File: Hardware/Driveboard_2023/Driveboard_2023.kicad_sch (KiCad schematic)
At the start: 15 parts

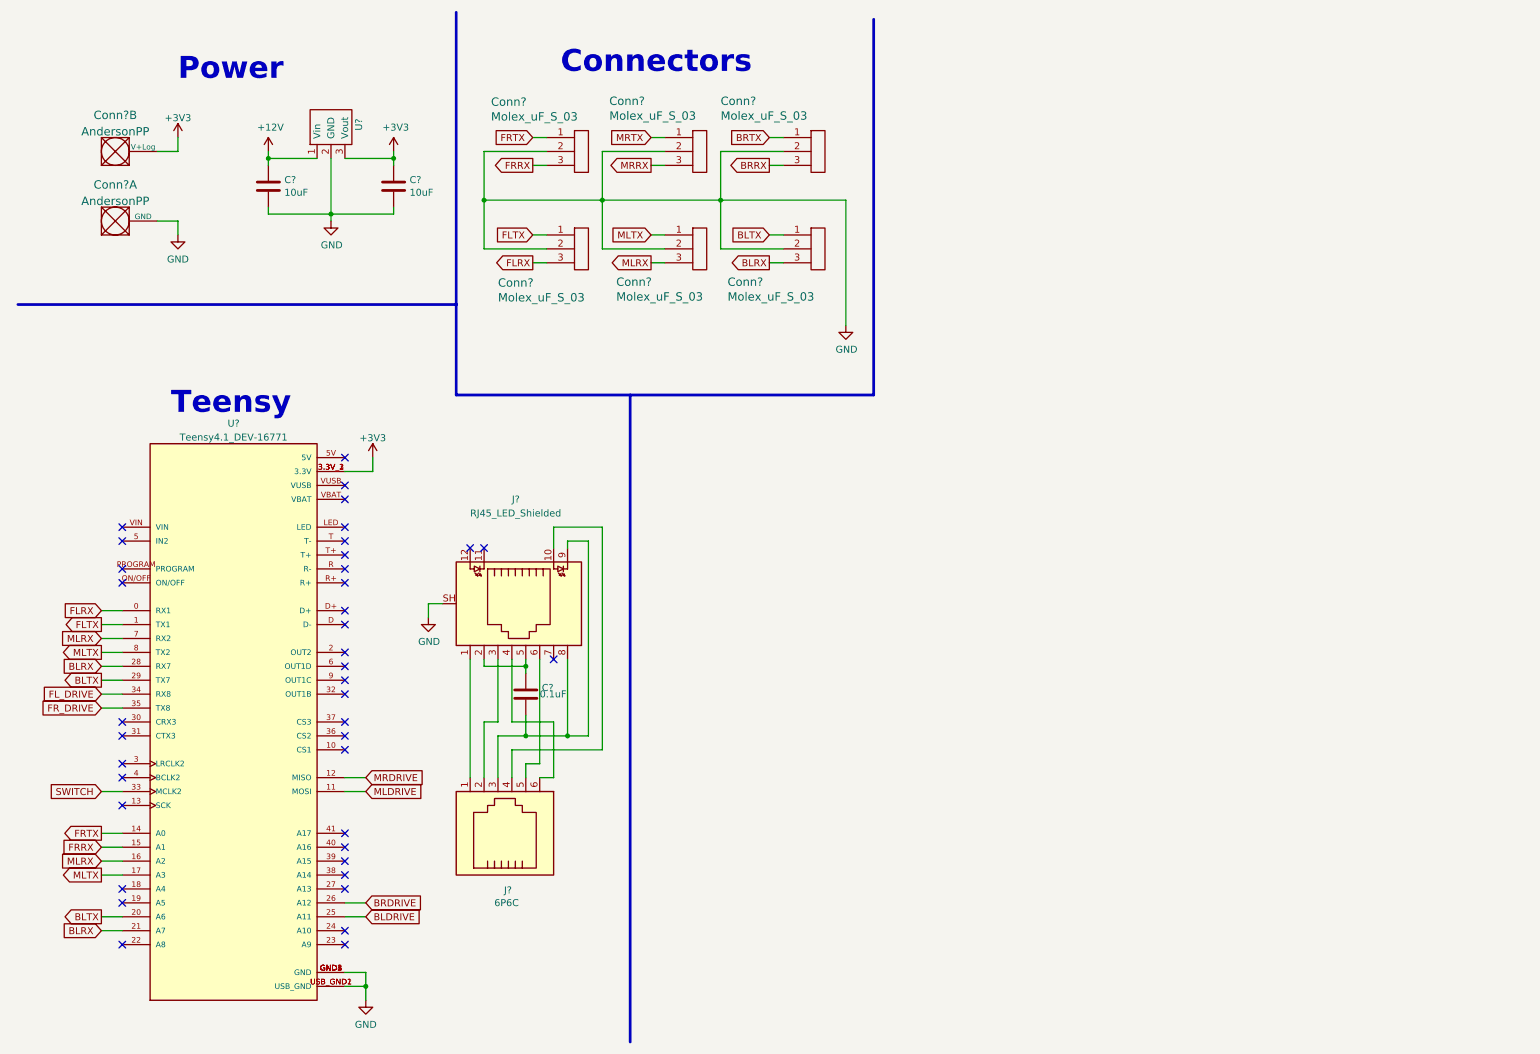
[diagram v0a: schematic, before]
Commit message: Finished Schematic for Review
Finished schematic for review
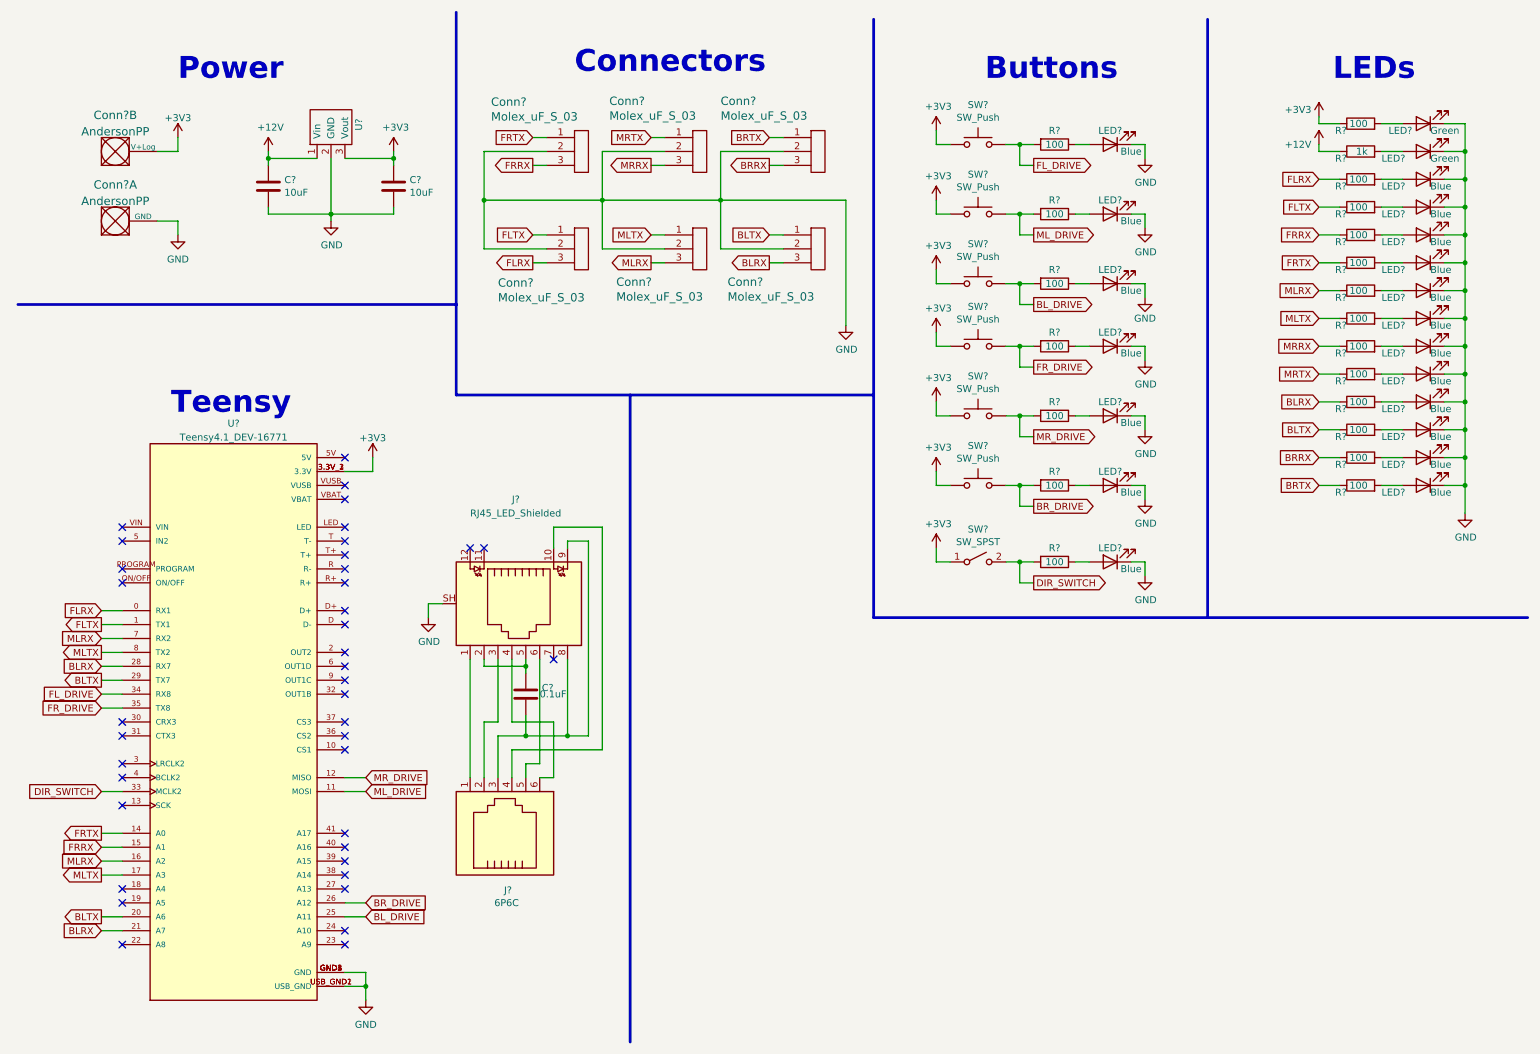
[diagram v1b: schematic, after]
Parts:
- added LED? (x19): Blue, LED_SMD:LED_0603_1608Metric_Pad1.05x0.95mm_HandSolder, symbol Device:LED
- added LED? (x2): Green, LED_SMD:LED_0603_1608Metric_Pad1.05x0.95mm_HandSolder, symbol Device:LED
- added R? (x20): 100, Resistor_SMD:R_0603_1608Metric_Pad0.98x0.95mm_HandSolder, symbol Device:R
- added R?: 1k, Resistor_SMD:R_0603_1608Metric_Pad0.98x0.95mm_HandSolder, symbol Device:R
- added SW? (x6): SW_Push, Button_Switch_SMD:SW_SPST_TL3305A, symbol Switch:SW_Push
- added SW?: SW_SPST, Button_Switch_THT:SW_Slide_1P2T_CK_OS102011MS2Q, symbol Switch:SW_SPST
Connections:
- net +12V: now also R?.1
- net +3V3: now also R?.1, SW?.1, SW?.1, SW?.1, SW?.1, SW?.1, SW?.1, SW?.1 (A)
- net BLRX: now also R?.1
- net BLTX: now also R?.1
- net BRRX: now also R?.1
- net BRTX: now also R?.1
- net FLRX: now also R?.1
- net FLTX: now also R?.1
- net FL_DRIVE: now also R?.2, SW?.2
- net FRRX: now also R?.1
- net FRTX: now also R?.1
- net FR_DRIVE: now also R?.2, SW?.2
- net GND: now also LED?.1 (K), LED?.1 (K), LED?.1 (K), LED?.1 (K), LED?.1 (K), LED?.1 (K), LED?.1 (K), LED?.1 (K), LED?.1 (K), LED?.1 (K), LED?.1 (K), LED?.1 (K), LED?.1 (K), LED?.1 (K), LED?.1 (K), LED?.1 (K), LED?.1 (K), LED?.1 (K), LED?.1 (K), LED?.1 (K), LED?.1 (K)
- net MLRX: now also R?.1
- net MLTX: now also R?.1
- net MRRX: now also R?.1
- net MRTX: now also R?.1
- net BLDRIVE renamed BL_DRIVE
- net BL_DRIVE: now also R?.2, SW?.2
- net BRDRIVE renamed BR_DRIVE
- net BR_DRIVE: now also R?.2, SW?.2
- net MLDRIVE renamed ML_DRIVE
- net ML_DRIVE: now also R?.2, SW?.2
- net MRDRIVE renamed MR_DRIVE
- net MR_DRIVE: now also R?.2, SW?.2
- net SWITCH renamed DIR_SWITCH
- net DIR_SWITCH: now also R?.2, SW?.2 (B)
- new net: LED?.2 (A), R?.1 (x7)
- new net: LED?.2 (A), R?.2 (x14)
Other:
- note added: "Buttons"
- note added: "LEDs"
